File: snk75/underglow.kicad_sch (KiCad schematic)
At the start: 34 parts, among them U3 74LVC1G125

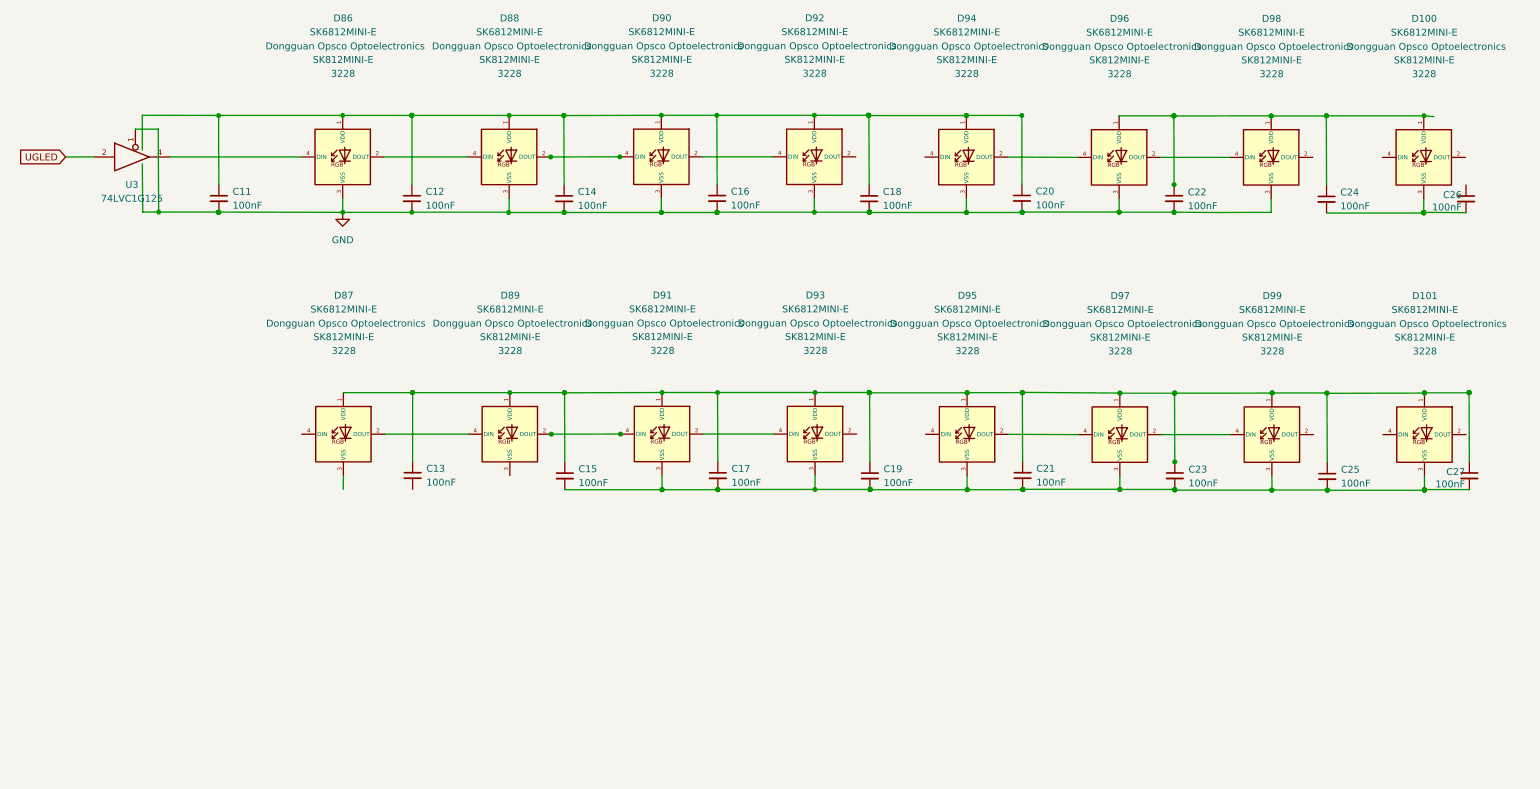
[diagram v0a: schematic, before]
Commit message: Changed MCU for STM32F072C8Tx and wired cols and rows
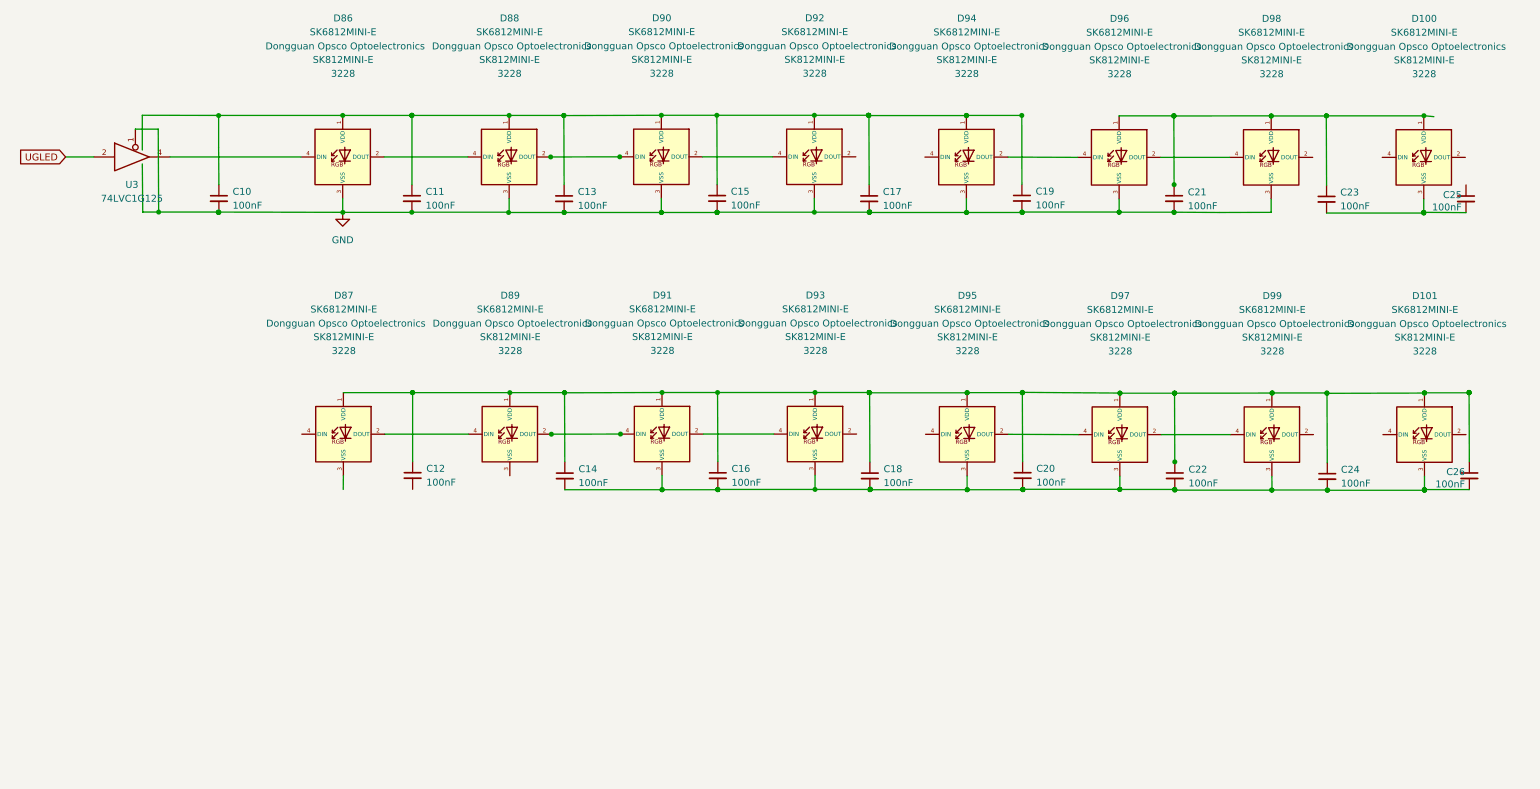
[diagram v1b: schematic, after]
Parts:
- C10: renamed from C11; footprint Capacitor_SMD:C_0805_2012Metric_Pad1.18x1.45mm_HandSolder -> Capacitor_SMD:C_0402_1005Metric
- C11: renamed from C12; footprint Capacitor_SMD:C_0805_2012Metric_Pad1.18x1.45mm_HandSolder -> Capacitor_SMD:C_0402_1005Metric
- C12: renamed from C13; footprint Capacitor_SMD:C_0805_2012Metric_Pad1.18x1.45mm_HandSolder -> Capacitor_SMD:C_0402_1005Metric
- C13: renamed from C14; footprint Capacitor_SMD:C_0805_2012Metric_Pad1.18x1.45mm_HandSolder -> Capacitor_SMD:C_0402_1005Metric
- C14: renamed from C15; footprint Capacitor_SMD:C_0805_2012Metric_Pad1.18x1.45mm_HandSolder -> Capacitor_SMD:C_0402_1005Metric
- C15: renamed from C16; footprint Capacitor_SMD:C_0805_2012Metric_Pad1.18x1.45mm_HandSolder -> Capacitor_SMD:C_0402_1005Metric
- C16: renamed from C17; footprint Capacitor_SMD:C_0805_2012Metric_Pad1.18x1.45mm_HandSolder -> Capacitor_SMD:C_0402_1005Metric
- C17: renamed from C18; footprint Capacitor_SMD:C_0805_2012Metric_Pad1.18x1.45mm_HandSolder -> Capacitor_SMD:C_0402_1005Metric
- C18: renamed from C19; footprint Capacitor_SMD:C_0805_2012Metric_Pad1.18x1.45mm_HandSolder -> Capacitor_SMD:C_0402_1005Metric
- C19: renamed from C20; footprint Capacitor_SMD:C_0805_2012Metric_Pad1.18x1.45mm_HandSolder -> Capacitor_SMD:C_0402_1005Metric
- C20: renamed from C21; footprint Capacitor_SMD:C_0805_2012Metric_Pad1.18x1.45mm_HandSolder -> Capacitor_SMD:C_0402_1005Metric
- C21: renamed from C22; footprint Capacitor_SMD:C_0805_2012Metric_Pad1.18x1.45mm_HandSolder -> Capacitor_SMD:C_0402_1005Metric
- C22: renamed from C23; footprint Capacitor_SMD:C_0805_2012Metric_Pad1.18x1.45mm_HandSolder -> Capacitor_SMD:C_0402_1005Metric
- C23: renamed from C24; footprint Capacitor_SMD:C_0805_2012Metric_Pad1.18x1.45mm_HandSolder -> Capacitor_SMD:C_0402_1005Metric
- C24: renamed from C25; footprint Capacitor_SMD:C_0805_2012Metric_Pad1.18x1.45mm_HandSolder -> Capacitor_SMD:C_0402_1005Metric
- C25: renamed from C26; footprint Capacitor_SMD:C_0805_2012Metric_Pad1.18x1.45mm_HandSolder -> Capacitor_SMD:C_0402_1005Metric
- C26: renamed from C27; footprint Capacitor_SMD:C_0805_2012Metric_Pad1.18x1.45mm_HandSolder -> Capacitor_SMD:C_0402_1005Metric
- D100, D101, D86, D87, D88, D89, D90, D91, D92, D93, D94, D95, D96, D97, D98, D99: footprint acheron_Components:SK6812MINI_3535_6028_3.2x2.8mm_Round -> LED_SMD:LED_SK6812MINI_PLCC4_3.5x3.5mm_P1.75mm
- U3: footprint (none) -> Package_TO_SOT_SMD:SOT-23-5_HandSoldering

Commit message: added new row layout and connected row1 to MCU
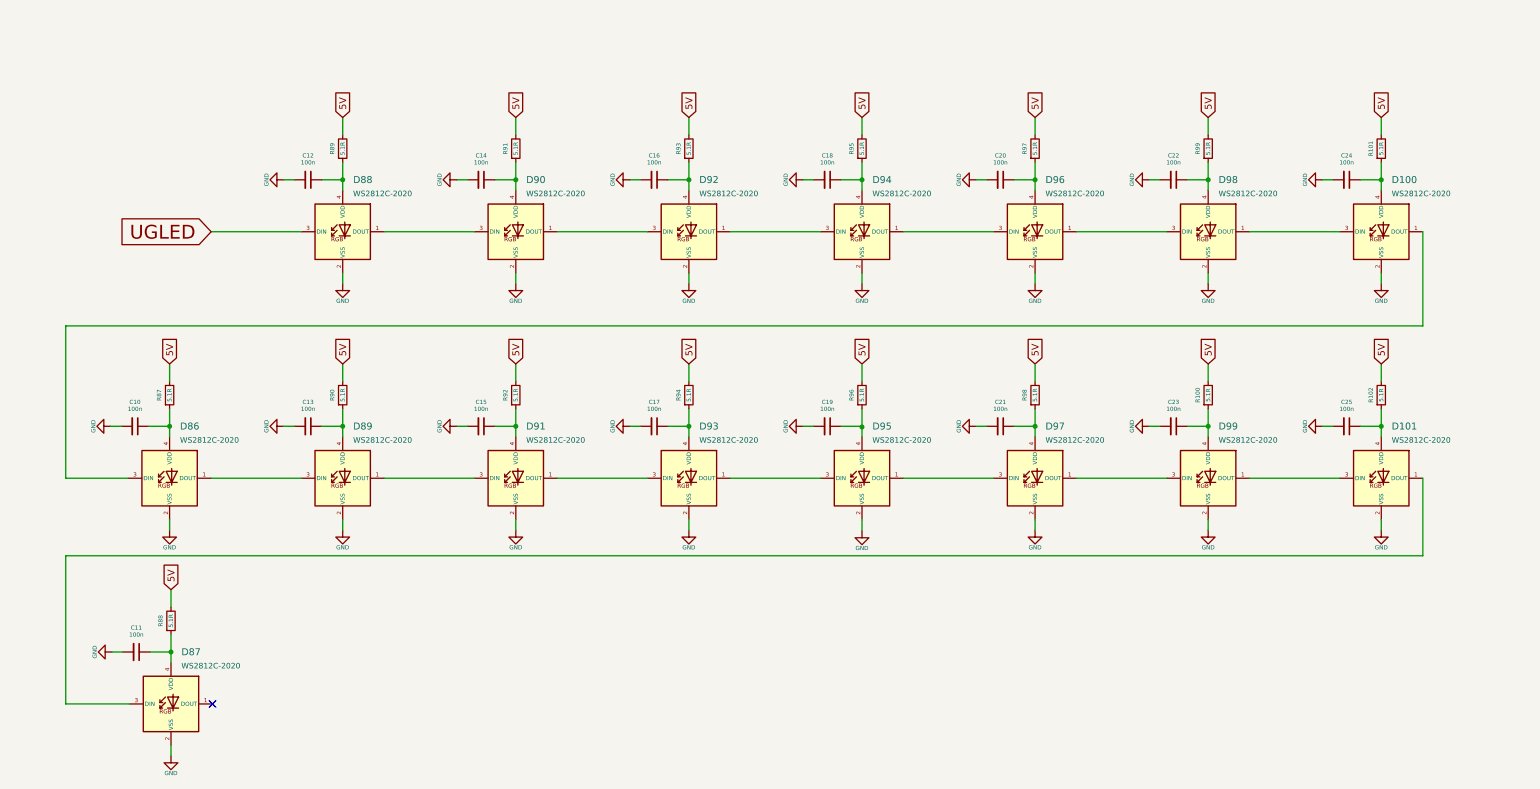
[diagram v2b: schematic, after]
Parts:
- removed C26: 100nF, Capacitor_SMD:C_0402_1005Metric, symbol Device:C_Small
- removed D100, D101, D86, D87, D88, D89, D90, D91, D92, D93, D94, D95, D96, D97, D98, D99: SK6812MINI-E, LED_SMD:LED_SK6812MINI_PLCC4_3.5x3.5mm_P1.75mm, symbol acheronSymbols:SK6812MINI-E
- removed U3: 74LVC1G125, Package_TO_SOT_SMD:SOT-23-5_HandSoldering, symbol 74xGxx:74LVC1G125
- added D100, D101, D86, D87, D88, D89, D90, D91, D92, D93, D94, D95, D96, D97, D98, D99: WS2812C-2020, acheron_Components:LED_WS2812_2020, symbol acheron_Symbols:WS2812B-2020
- added R100, R101, R102, R87, R88, R89, R90, R91, R92, R93, R94, R95, R96, R97, R98, R99: 5.1R, Resistor_SMD:R_0402_1005Metric, symbol Device:R_Small
- C10, C11, C12, C13, C14, C15, C16, C17, C18, C19, C20, C21, C22, C23, C24, C25: value 100nF -> 100n; Manufacturer (none) -> Samsung; Manufacturer Part Number (none) -> CL05B104KB54PNC; Package (none) -> C0402; Specification (none) -> 50V 100nF X7R ±10% 0402 MLCC; Vendor Part Number (none) -> LCSC C307331
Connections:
- net GND: now also C11.2, C12.2, C13.2, C14.2, C15.2, C16.2, C17.2, C18.2, C19.2, C20.2, C21.2, C22.2, C23.2, C24.2, C25.2, D100.2 (VSS), D101.2 (VSS), D86.2 (VSS), D87.2 (VSS), D88.2 (VSS), D89.2 (VSS), D90.2 (VSS), D91.2 (VSS), D92.2 (VSS), D93.2 (VSS), D94.2 (VSS), D95.2 (VSS), D96.2 (VSS), D97.2 (VSS), D98.2 (VSS), D99.2 (VSS)
- net UGLED: now also D88.3 (DIN)
- net at C20.1: now also D96.4 (VDD), R97.1
- net at C15.1: now also D91.4 (VDD), R92.1; no longer C13.1
- net at C24.1: now also D100.4 (VDD), R101.1
- net at C23.1: now also D99.4 (VDD), R100.1
- net at C16.1: now also D92.4 (VDD), R93.1; no longer C14.1
- net at C12.1: now also D88.4 (VDD), R89.1
- net at C25.1: now also D101.4 (VDD), R102.1
- net at C19.1: now also R96.1
- net at C22.1: now also D98.4 (VDD), R99.1
- net at C17.1: now also D93.4 (VDD), R94.1
- net at C21.1: now also D97.4 (VDD), R98.1
- net at C18.1: now also D94.4 (VDD), R95.1
- net at C10.1: now also D86.4 (VDD), R87.1
- net VCC: no longer names the net of C11.1
- net VCC: now also D87.4 (VDD), R88.1
- new net: D96.1 (DOUT), D98.3 (DIN)
- new net: D94.1 (DOUT), D96.3 (DIN)
- new net: C14.1, D90.4 (VDD), R91.1
- new net: D100.3 (DIN), D98.1 (DOUT)
- new net: D86.1 (DOUT), D89.3 (DIN)
- new net: D100.1 (DOUT), D86.3 (DIN)
- new net: D92.1 (DOUT), D94.3 (DIN)
- new net: D90.1 (DOUT), D92.3 (DIN)
- new net: D101.1 (DOUT), D87.3 (DIN)
- new net: D91.1 (DOUT), D93.3 (DIN)
- new net: D89.1 (DOUT), D91.3 (DIN)
- new net: D101.3 (DIN), D99.1 (DOUT)
- new net: D88.1 (DOUT), D90.3 (DIN)
- new net: D93.1 (DOUT), D95.3 (DIN)
- new net: D95.1 (DOUT), D97.3 (DIN)
- new net: D97.1 (DOUT), D99.3 (DIN)
- new net: C13.1, D89.4 (VDD), R90.1
- new net 5V: R100.2, R101.2, R102.2, R87.2, R88.2, R89.2, R90.2, R91.2, R92.2, R93.2, R94.2, R95.2, R96.2, R97.2, R98.2, R99.2
- no-connect marks 0 -> 1
